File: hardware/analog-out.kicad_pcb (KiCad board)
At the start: 2 copper layers, 30 x 30 mm, 30 parts, among them P1 CON-SENSOR, P2 AKL_5_2, P3 AKL_5_2, U1 M24C64, U2 MCP4725A0, U3 TLV272IS, U4 DRILL, U5 DRILL, U6 DRILL, U7 DRILL

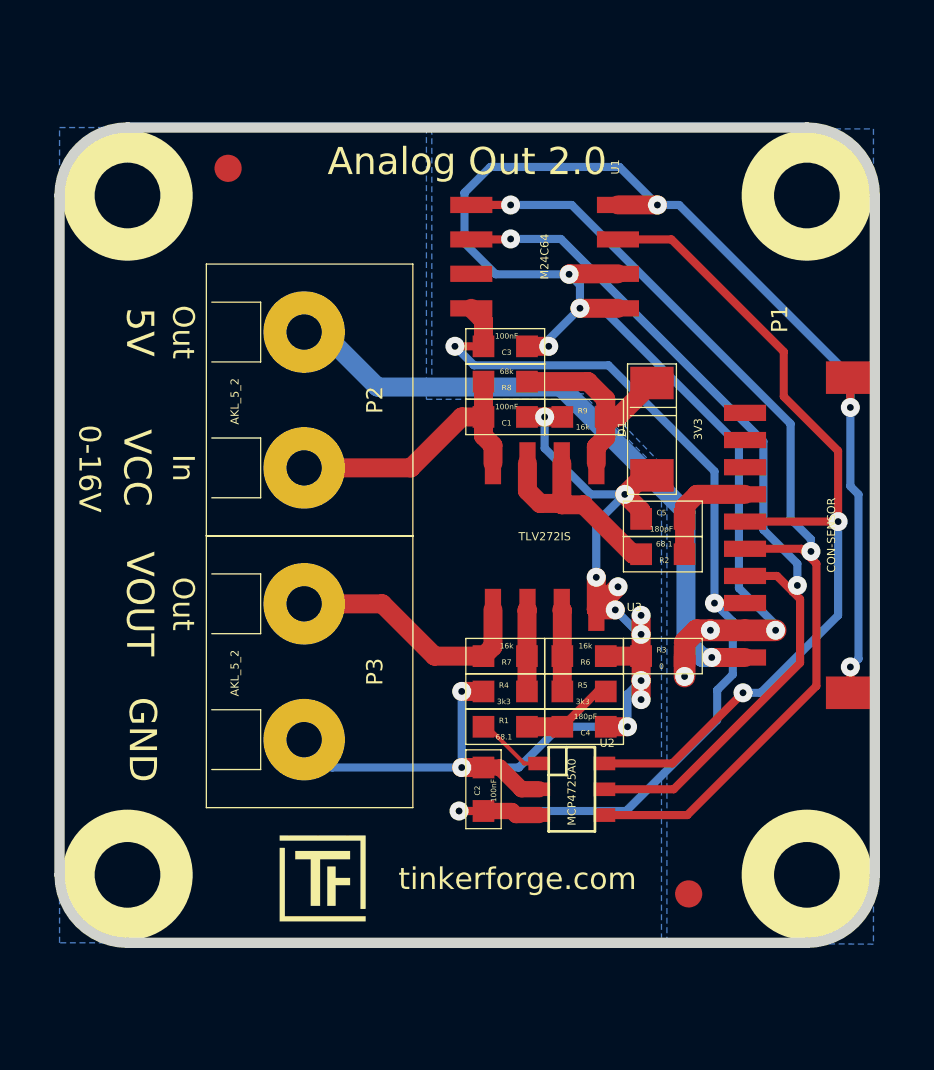
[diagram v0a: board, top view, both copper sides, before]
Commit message: change output voltage to max 12V
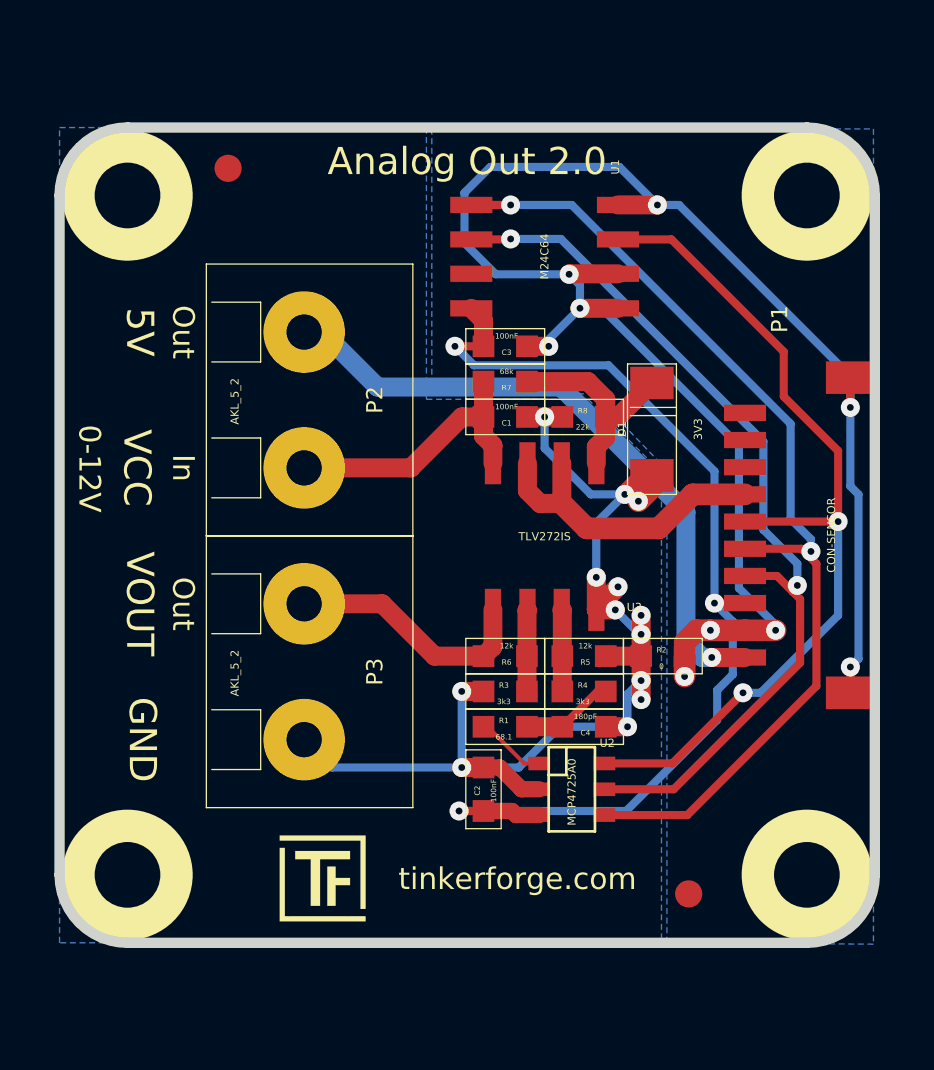
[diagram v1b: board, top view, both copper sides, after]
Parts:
- removed C5: 180pF, 0603
- removed R9: 16k, 0603
- R2: value 68.1 -> 0
- R3: value 0 -> 3k3
- R5: value 3k3 -> 12k
- R6: value 16k -> 12k
- R7: value 16k -> 68k
- R8: value 68k -> 22k
- moved R7 10.1 mm to (154.4, 94.4)
- moved R3 5.94 mm to (154.4, 105.8)
- moved R2 3.75 mm to (160.2, 104.5), turned to 180 degrees
- moved R8 3.18 mm to (157.3, 95.7), turned to 180 degrees
- moved R4 2.90 mm to (157.3, 105.8)
- moved R6 2.90 mm to (154.4, 104.5)
- moved R5 1.30 mm to (157.3, 104.5), turned to 0 degrees
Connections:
- P1 pad 7: Net-(C5-Pad1) -> Net-(P1-Pad7)
- R2 pad 1: Net-(R2-Pad1) -> GND
- R2 pad 2: Net-(C5-Pad1) -> AGND
- R3 pad 1: GND -> Net-(R3-Pad1)
- R4 pad 1: Net-(R4-Pad1) -> Net-(C4-Pad1)
- R4 pad 2: AGND -> Net-(R4-Pad2)
- R5 pad 1: Net-(C4-Pad1) -> Net-(R4-Pad2)
- R5 pad 2: Net-(R5-Pad2) -> AGND
- R6 pad 1: Net-(R5-Pad2) -> Net-(P3-Pad2)
- R6 pad 2: AGND -> Net-(R3-Pad1)
- R7 pad 1: Net-(P3-Pad2) -> VCC
- R7 pad 2: Net-(R4-Pad1) -> Net-(D1-Pad2)
- R8 pad 1: VCC -> Net-(D1-Pad2)
- R8 pad 2: Net-(D1-Pad2) -> AGND
- U3 pad 2: Net-(R4-Pad1) -> Net-(R3-Pad1)
- U3 pad 3: Net-(R5-Pad2) -> Net-(R4-Pad2)
- U3 pad 6: Net-(R2-Pad1) -> Net-(P1-Pad7)
- U3 pad 7: Net-(R2-Pad1) -> Net-(P1-Pad7)
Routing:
- net Net-(P1-Pad7): track 0.00 -> 11.6 mm
- net Net-(R2-Pad1): track 7.67 -> 0.00 mm
- net Net-(C5-Pad1): track 4.16 -> 0.00 mm
- net Net-(R5-Pad2): track 3.01 -> 0.00 mm
- net Net-(R4-Pad2): track 0.00 -> 3.01 mm
- net Net-(R3-Pad1): track 0.00 -> 3.01 mm
- net Net-(R4-Pad1): track 3.01 -> 0.00 mm
- net AGND: vias 12 -> 13
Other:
- board text added: "0-12V"
- board text removed: "0-16V"

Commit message: add second ground connector add fuse and z-diode for 5V rail
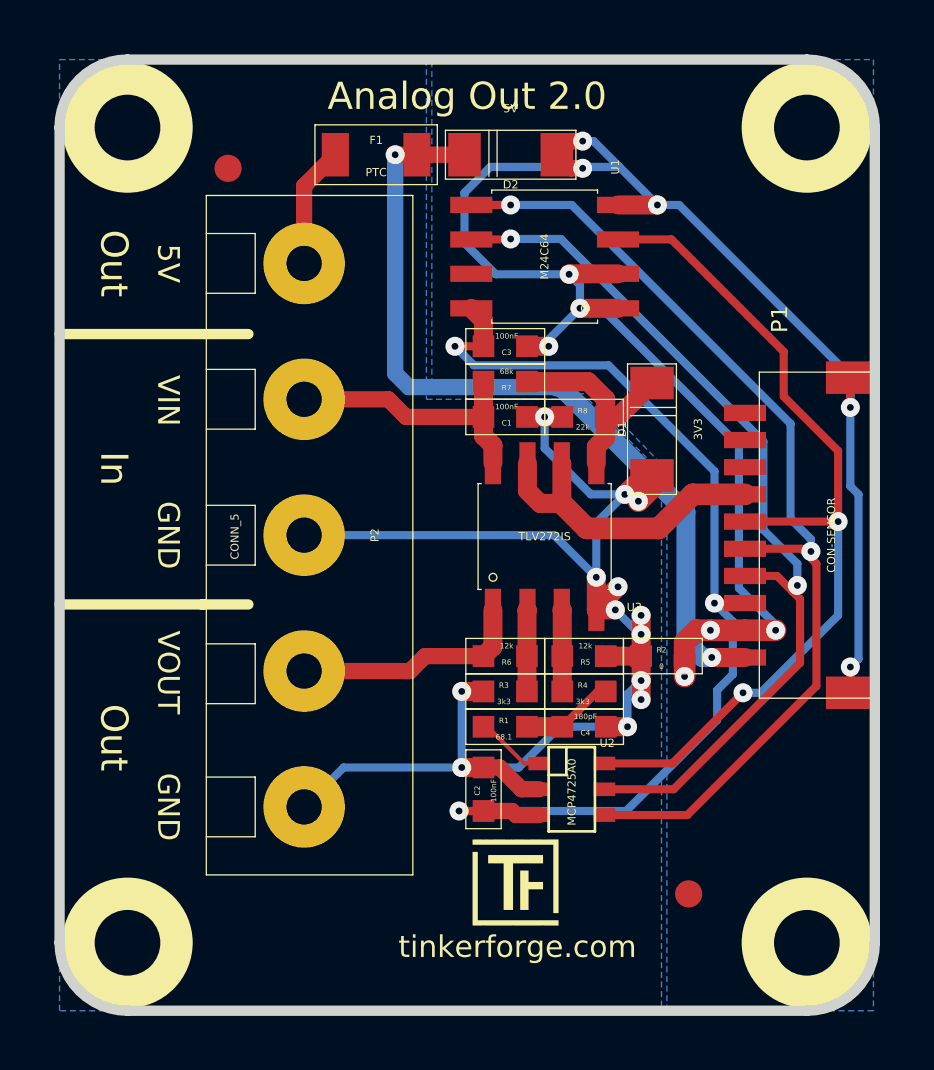
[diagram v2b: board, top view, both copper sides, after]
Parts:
- removed P3: AKL_5_2, AKL_5_2
- added D2: 5V, kicad-libraries:MiniMelf, F.Cu at (154.7, 86.1)
- added F1: PTC, kicad-libraries:1206, F.Cu at (149.7, 86.1)
- C1, C2, C3, C4, R1, R2, R3, R4, R5, R6, R7, R8: footprint 0603 -> kicad-libraries:0603
- P1: footprint CON-SENSOR -> kicad-libraries:CON-SENSOR
- P2: value AKL_5_2 -> CONN_5; footprint AKL_5_2 -> kicad-libraries:AKL_5_5
- U1, U3: footprint SOIC8 -> kicad-libraries:SOIC8
- U2: footprint SOT23-6 -> kicad-libraries:SOT23-6
- U4, U5, U6, U7: footprint DRILL_NP -> kicad-libraries:DRILL_NP
- moved Ref** 7.10 mm to (153.2, 111.3)
- moved P2 4.97 mm to (147.1, 100.1)
- moved U4 2.50 mm to (165.6, 115.1)
- moved U5 2.50 mm to (140.6, 115.1)
- moved U6 2.50 mm to (140.6, 85.1)
- moved U7 2.50 mm to (165.6, 85.1)
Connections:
- P2 pad 1: VCC -> AGND
- P2 pad 2: +5V -> Net-(P2-Pad2)
- R6 pad 1: Net-(P3-Pad2) -> Net-(P2-Pad2)
- U3 pad 1: Net-(P3-Pad2) -> Net-(P2-Pad2)
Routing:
- net AGND: track 43.3 -> 54.8 mm
- net Net-(P3-Pad2): track 9.24 -> 0.00 mm
- net Net-(P2-Pad2): track 0.00 -> 8.67 mm
- net +5V: track 24.0 -> 30.6 mm, vias 1 -> 2
- net Net-(F1-Pad2): track 0.00 -> 5.18 mm
- net GND: track 65.8 -> 69.9 mm, vias 9 -> 11
- net VCC: track 10.5 -> 10.0 mm
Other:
- board size 30 x 30 mm -> 30 x 35 mm
- board text added: "VIN"
- board text removed: "0-12V"
- board text removed: "VCC"
